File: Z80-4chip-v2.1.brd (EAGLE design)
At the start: 99.7 x 99.7 mm, 100 parts, among them IC1 Z84C00xx (-Z80-), IC2 CXK581000 (128k * 8), IC4 7400N, M1 WIRE-VIA8, U1 ATMEGA32A-PU

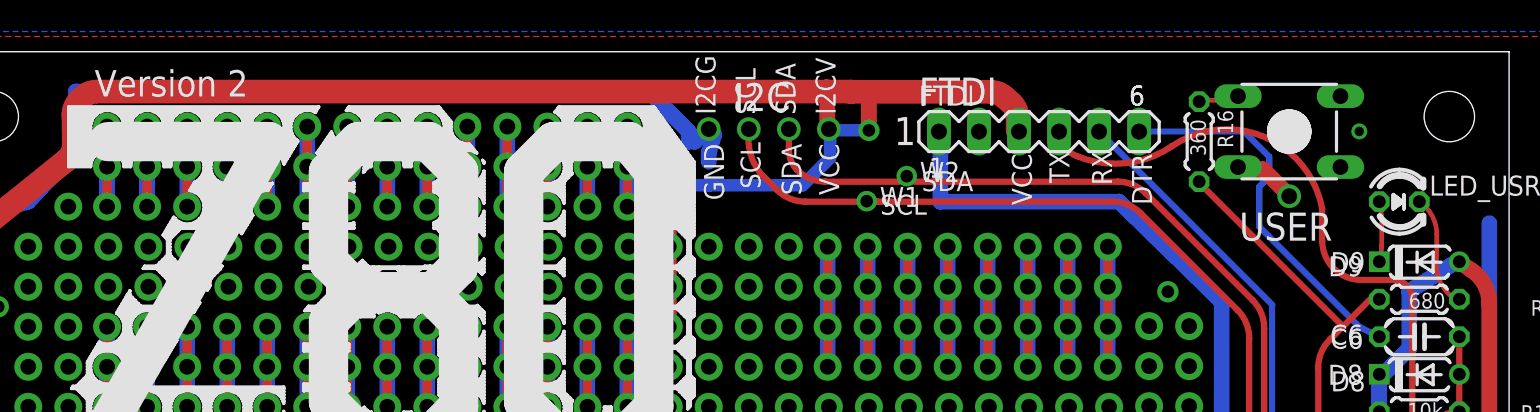
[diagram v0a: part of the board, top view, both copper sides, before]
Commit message: Add VCC/GND labels to bottom silk for new prototype-area vias. Bump version to V2.1 to account for the new power vias in prototype area. rename files to reflect version number (Z80-4chip-v2.1.*) Add zip of v2.1 gerbers to Gerbers-V2 directory.
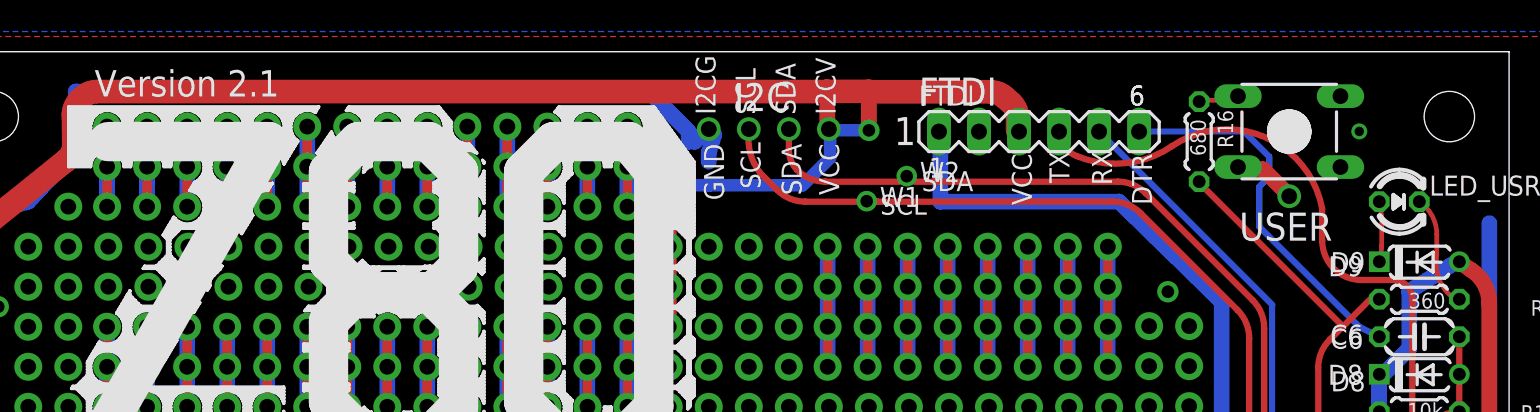
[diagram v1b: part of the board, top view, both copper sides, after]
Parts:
- R16: value 360 -> 680
- R17: value 680 -> 360
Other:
- board text added: "20171114 by WestfW: Make sure R16/R17 values are correct in sch and silkscreen."
- board text added: "20171114 by WestfW: resync to github, adjust bottom silkscreen for new power vias, bump to "Version 2.1""
- board text added: "Version 2.1"
- board text removed: "Version 2"
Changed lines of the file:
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@@
 <layer number="14" name="Route14" color="1" fill="6" visible="no" active="no"/>
 <layer number="15" name="Route15" color="4" fill="6" visible="no" active="no"/>
-<layer number="16" name="Bottom" color="1" fill="1" visible="no" active="yes"/>
+<layer number="16" name="Bottom" color="1" fill="1" visible="yes" active="yes"/>
 <layer number="17" name="Pads" color="2" fill="1" visible="yes" active="yes"/>
 <layer number="18" name="Vias" color="2" fill="1" visible="yes" active="yes"/>
@@
 <layer number="116" name="Patch_BOT" color="7" fill="1" visible="no" active="yes"/>
 <layer number="118" name="Rect_Pads" color="7" fill="1" visible="no" active="no"/>
-<layer number="121" name="_tSilk" color="6" fill="1" visible="no" active="yes"/>
+<layer number="121" name="_tSilk" color="6" fill="1" visible="yes" active="yes"/>
 <layer number="122" name="_bplace" color="14" fill="1" visible="no" active="yes"/>
 <layer number="123" name="tTestmark" color="7" fill="1" visible="no" active="yes"/>
@@
 <rectangle x1="59.055" y1="51.7525" x2="60.325" y2="53.34" layer="30"/>
 <text x="-3.01615" y="39.694415625" size="1.27" layer="100" font="fixed" ratio="12">20170228 by WestfW: "version 2" in silkscreen</text>
-<text x="10.556875" y="96.8375" size="1.6764" layer="121" ratio="16">Version 2</text>
-<wire x1="45.72" y1="81.835625" x2="45.72" y2="87.9475" width="0.6" layer="122"/>
-<wire x1="45.72" y1="87.9475" x2="46.355" y2="88.5825" width="0.6" layer="122"/>
-<wire x1="46.355" y1="88.5825" x2="47.704375" y2="88.5825" width="0.6" layer="122"/>
-<wire x1="47.704375" y1="88.5825" x2="48.339375" y2="87.9475" width="0.6" layer="122"/>
-<wire x1="48.339375" y1="87.9475" x2="48.339375" y2="81.518125" width="0.6" layer="122"/>
+<text x="10.556875" y="96.8375" size="1.6764" layer="121" ratio="16">Version 2.1</text>
+<wire x1="45.72" y1="81.835625" x2="45.72" y2="90.805" width="0.6" layer="122"/>
+<wire x1="45.72" y1="90.805" x2="46.0375" y2="91.28125" width="0.6" layer="122"/>
+<wire x1="46.0375" y1="91.28125" x2="47.9425" y2="91.28125" width="0.6" layer="122"/>
+<wire x1="47.9425" y1="91.28125" x2="48.339375" y2="90.805" width="0.6" layer="122"/>
+<wire x1="48.339375" y1="90.805" x2="48.339375" y2="81.518125" width="0.6" layer="122"/>
 <wire x1="48.339375" y1="81.518125" x2="47.863125" y2="81.041875" width="0.6" layer="122"/>
 <wire x1="47.863125" y1="81.041875" x2="47.625" y2="80.9625" width="0.6" layer="122"/>
@@
 <text x="-3.01615" y="42.075665625" size="1.27" layer="100" font="fixed" ratio="12">20170512 by WestfW: Put some power and Gnd vias near the prototype area!</text>
 <text x="-1.984375" y="90.090625" size="1.6764" layer="102" ratio="14">R16 and R17 have the values swapped</text>
+<text x="47.9425" y="96.99625" size="1.778" layer="122" font="vector" ratio="12" rot="MR270">VCC</text>
+<text x="46.116875" y="68.183125" size="1.778" layer="122" font="vector" ratio="12" rot="MR90">GND</text>
+<text x="-3.095525" y="44.298165625" size="1.27" layer="100" font="fixed" ratio="12">20171114 by WestfW: resync to github, adjust bottom silkscreen for new power vias, bump to "Version 2.1"</text>
+<text x="-3.01615" y="46.520665625" size="1.27" layer="100" font="fixed" ratio="12">20171114 by WestfW: Make sure R16/R17 values are correct in sch and silkscreen.</text>
 </plain>
 <attributes>
@@
 <attribute name="VALUE" x="7.30280625" y="27.686" size="1.27" layer="27" ratio="10" rot="R180"/>
 </element>
-<element name="R16" library="my-rcl" package="0204/5" value="360" x="80.645" y="93.98" smashed="yes" rot="R270">
+<element name="R16" library="my-rcl" package="0204/5" value="680" x="80.645" y="93.98" smashed="yes" rot="R270">
 <attribute name="NAME" x="81.8134" y="95.9866" size="0.9906" layer="25" ratio="12" rot="R270"/>
 <attribute name="VALUE" x="80.080409375" y="95.398996875" size="0.9906" layer="121" ratio="12" rot="R270"/>
 </element>
-<element name="R17" library="my-rcl" package="0204/5" value="680" x="94.615" y="83.97875" smashed="yes" rot="R180">
+<element name="R17" library="my-rcl" package="0204/5" value="360" x="94.615" y="83.97875" smashed="yes" rot="R180">
 <attribute name="NAME" x="104.0852375" y="83.921953125" size="0.9906" layer="25" ratio="12" rot="R180"/>
 <attribute name="VALUE" x="96.272196875" y="84.384540625" size="0.9906" layer="121" ratio="12" rot="R180"/>
@@
 <contactref element="D8" pad="C"/>
 <wire x1="19.05" y1="43.815" x2="16.51" y2="43.815" width="1" layer="16"/>
-<wire x1="58.59749375" y1="97.155" x2="57.0094875" y2="97.155" width="1.5" layer="1"/>
 <wire x1="57.0094875" y1="97.155" x2="10.68605" y2="97.155" width="1.5" layer="1"/>
 <wire x1="10.68605" y1="97.155" x2="9.788025" y2="96.783025" width="1.5" layer="1" curve="45"/>
@@
 <wire x1="57.05" y1="97.17" x2="57.05" y2="94.944003125" width="1" layer="1"/>
 <wire x1="57.05" y1="94.944003125" x2="57.15" y2="94.774003125" width="1" layer="1"/>
-<wire x1="58.45" y1="97.1412" x2="58.59749375" y2="97.1412" width="1.5" layer="1"/>
-<wire x1="58.59749375" y1="97.1412" x2="59.84875" y2="97.1412" width="1.5" layer="1"/>
 <wire x1="59.84875" y1="97.1412" x2="67.424721875" y2="97.1412" width="1.5" layer="1"/>
 <wire x1="67.424721875" y1="97.1412" x2="68.25850625" y2="96.82916875" width="1.5" layer="1" curve="-41.035235"/>
@@
 <wire x1="42.19381875" y1="5.399228125" x2="42.2410125" y2="5.352034375" width="1" layer="1"/>
 <wire x1="42.2410125" y1="5.352034375" x2="42.2410125" y2="2.54" width="1" layer="1"/>
-<wire x1="58.59749375" y1="97.155" x2="58.59749375" y2="97.1412" width="1.5" layer="1"/>
 <wire x1="57.05" y1="97.17" x2="57.0094875" y2="97.17" width="1.5" layer="1"/>
 <wire x1="57.0094875" y1="97.17" x2="57.0094875" y2="97.155" width="1.5" layer="1"/>
@@
 <wire x1="59.69" y1="97.1412" x2="59.84875" y2="97.1412" width="0.8" layer="1"/>
 <wire x1="57.229375" y1="94.694375" x2="59.769375" y2="94.694375" width="0.8" layer="16"/>
+<wire x1="57.05" y1="97.17" x2="59.69" y2="97.17" width="1.5" layer="1"/>
+<wire x1="59.69" y1="97.17" x2="59.69" y2="97.1412" width="1.5" layer="1"/>
 </signal>
 <signal name="GND" class="1">
